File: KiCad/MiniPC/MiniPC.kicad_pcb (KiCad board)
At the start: 4 copper layers, 167.6 x 83.8 mm, 57 parts, among them J1 GPIO, SW1 SW_Push_45deg, SW10 SW_Push_45deg, SW11 SW_Push_45deg, SW12 SW_Push_45deg, SW13 SW_Push_45deg, SW14 SW_Push_45deg, SW15 SW_Push_45deg, SW16 SW_Push_45deg, SW17 SW_Push_45deg, SW18 SW_Push_45deg, SW2 SW_Push_45deg, SW20 SW_Push_45deg, SW21 SW_Push_45deg, SW22 SW_Push_45deg, SW3 SW_Push_45deg, SW4 SW_Push_45deg, SW5 SW_Push_45deg, SW6 SW_Push_45deg, SW7 SW_Push_45deg, SW8 SW_Push_45deg, SW9 SW_Push_45deg, U1 DFRobot DFR0647, U3 Adafruit 5628, U5 MCP3008

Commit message: Kicad 27.07
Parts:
- J1: moved to B.Cu
- moved D10 27.2 mm to (202.4, 83.7), turned to 180 degrees
- moved D13 23.0 mm to (312.1, 75.6), turned to 0 degrees
- moved D12 5.08 mm to (319.7, 145.7)
- moved D11 3.52 mm to (299.1, 136.8)
- moved D14 3.52 mm to (311.8, 115.2)
- moved D16 3.52 mm to (299.1, 82.2)
- moved D17 3.52 mm to (311.8, 82.2)
- moved SW11 3.52 mm to (294.2, 115.2)
- moved SW13 3.52 mm to (338.5, 70.8)
- moved SW16 3.52 mm to (300.2, 87.3)
- moved SW17 3.52 mm to (312.9, 87.3)
- moved D15 3.52 mm to (329.6, 136.8)
- moved D18 3.52 mm to (324.5, 82.2)
- moved SW12 3.52 mm to (309.5, 130.5)
- moved SW14 3.52 mm to (309.5, 100.0)
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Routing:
- net /GPIO3/SCL1: track 67.4 -> 110.7 mm
- net /GPIO25: track 179.5 -> 222.0 mm, vias 0 -> 1
- net Net-(D10-A): track 62.3 -> 29.6 mm
- net /GPIO2/SDA1: track 69.5 -> 101.1 mm
- net Net-(D13-A): track 47.0 -> 21.5 mm
- net /GPIO17: track 16.6 -> 28.4 mm
- net /ID_SDA: track 62.4 -> 70.7 mm, vias 0 -> 1
- net GNDA: track 101.3 -> 94.7 mm
- net /GPIO6: track 78.1 -> 84.1 mm
- net /GPIO11/SPI0.SCLK: track 38.6 -> 44.5 mm, vias 0 -> 1
- net /GPIO22: track 103.0 -> 97.4 mm
- net /GPIO9/SPI0.MISO: track 35.0 -> 40.3 mm, vias 0 -> 1
- net /GPIO10/SPI0.MOSI: track 31.4 -> 36.5 mm, vias 0 -> 1
- net /GPIO13/PWM1: track 184.9 -> 189.9 mm
- net /GPIO24: track 251.4 -> 256.3 mm
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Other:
- board size 167.6 x 83.8 mm -> 171.4 x 83.8 mm

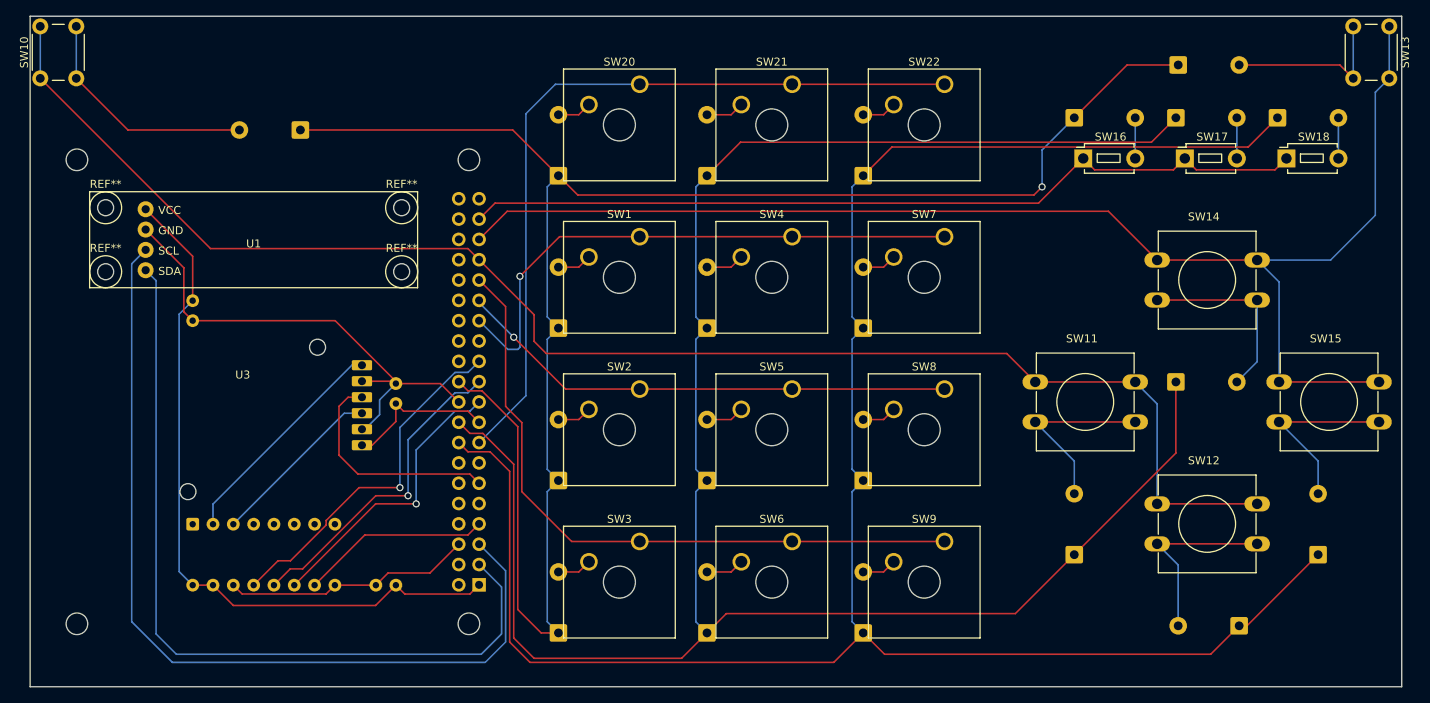
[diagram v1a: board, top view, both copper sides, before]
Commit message: Kicad 28.07
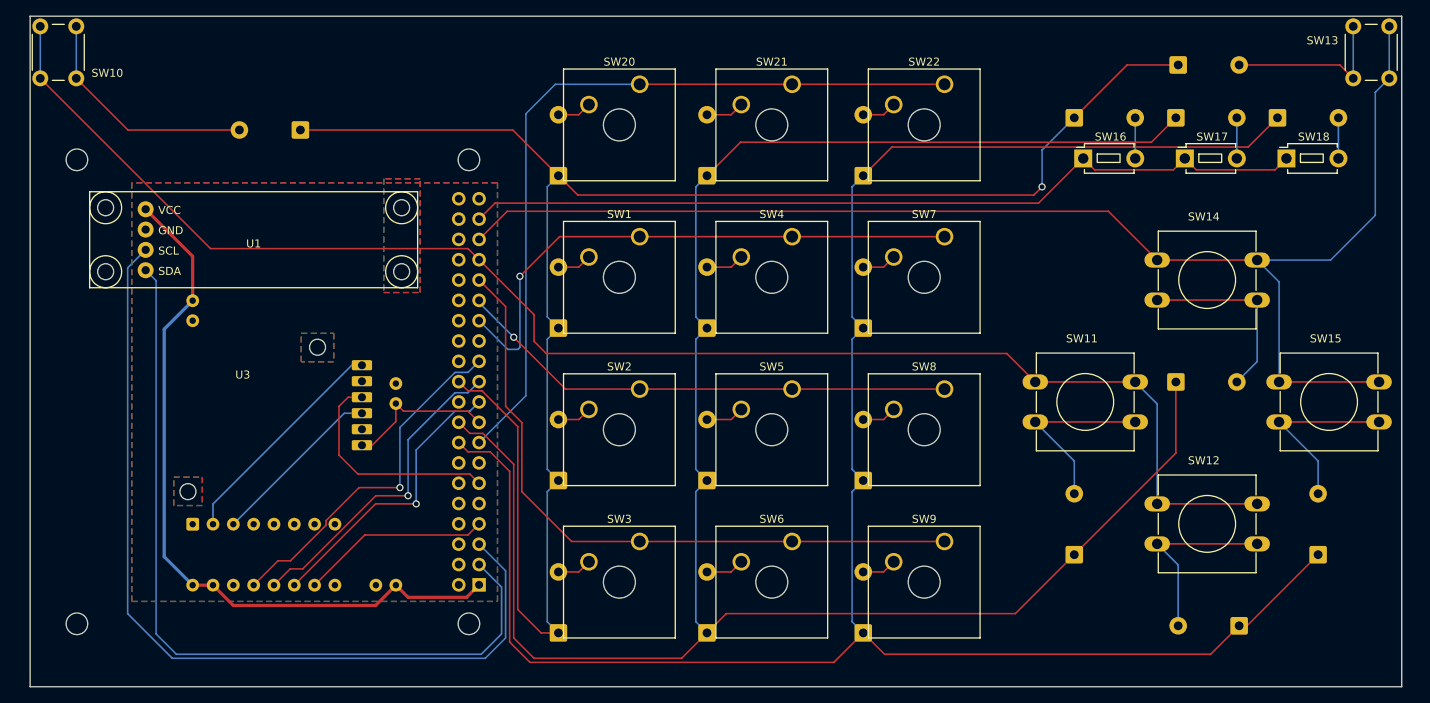
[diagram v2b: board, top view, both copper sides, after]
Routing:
- net GNDA: track 94.7 -> 1.07 mm
- net +3V3: track 108.7 -> 110.6 mm
- net /GPIO3/SCL1: track 110.7 -> 110.1 mm
- added copper zone on B.Cu, net (none)
- added copper zone on F.Cu, net (none)
- added copper zone on B.Cu, net GNDA
- added copper zone on F.Cu, net GNDA
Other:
- copper layers 4 -> 2
